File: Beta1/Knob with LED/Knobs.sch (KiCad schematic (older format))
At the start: 16 parts, among them U1000 MCP3008T-I/SL

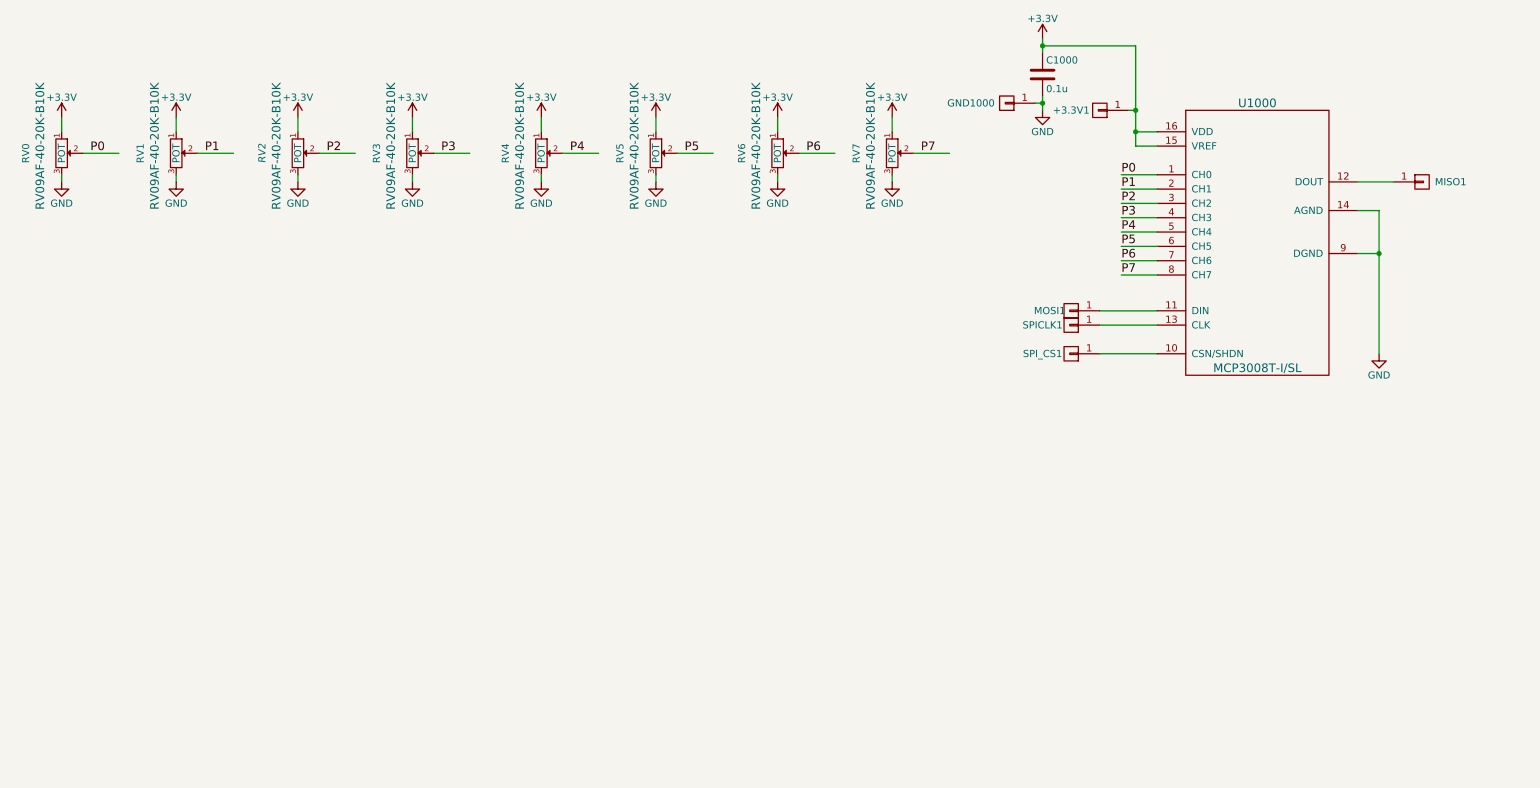
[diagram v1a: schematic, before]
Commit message: Duplicated row. Placed components and drill holes. Ready to be routed.
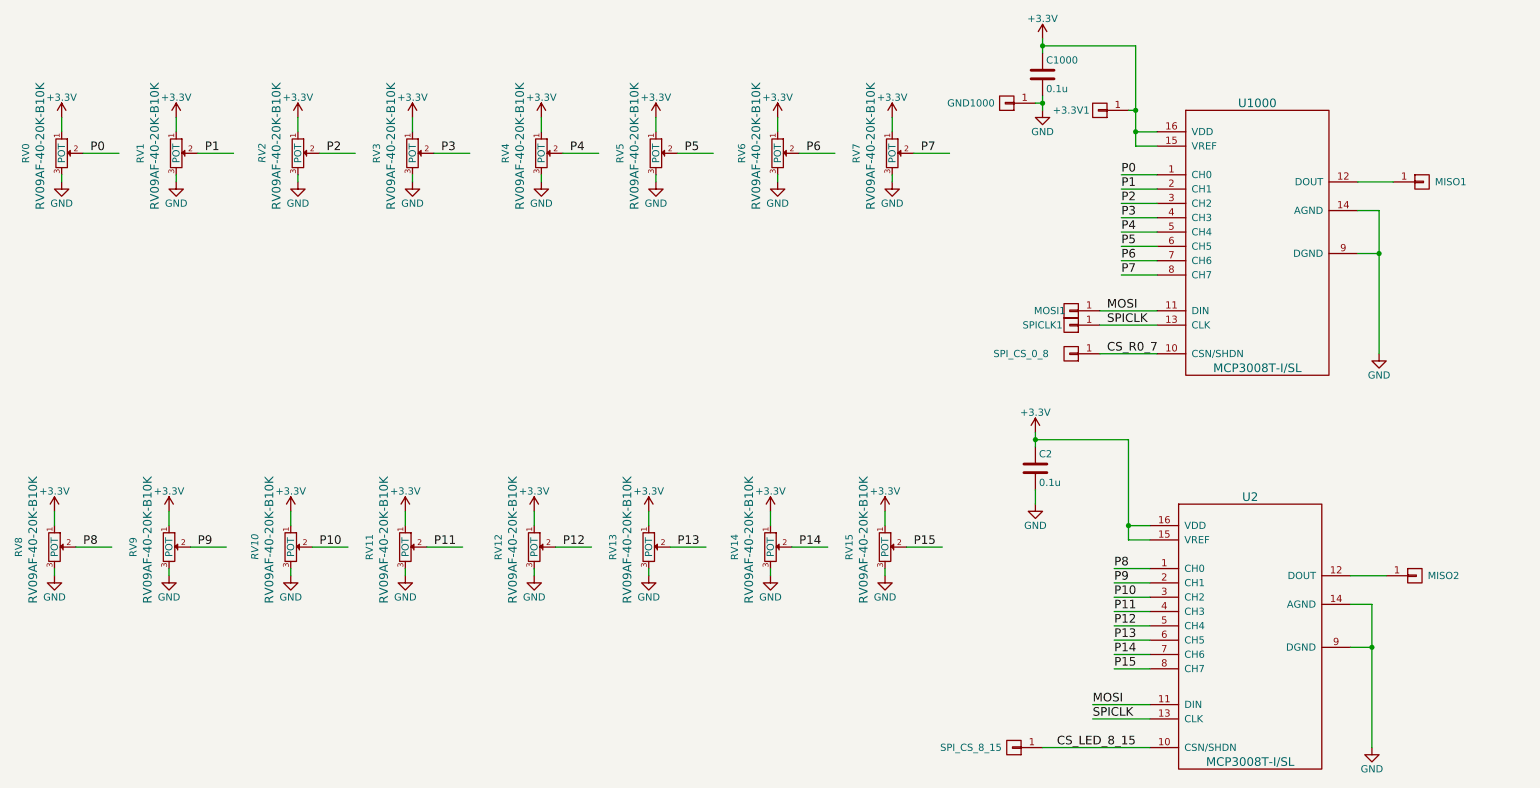
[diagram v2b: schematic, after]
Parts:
- added C2: 0.1u, Capacitors_SMD:C_0603, symbol C
- added MISO2, SPI_CS_8_15: CONN_01X01, Liberry:single_0.1, symbol CONN_01X01
- added RV10, RV11, RV12, RV13, RV14, RV15, RV8, RV9: POT, Liberry:RV09AF-40-20K-B10K, symbol POT
- added U2: MCP3008T-I/SL, Liberry:SOIC-16, symbol MCP3008T-I/SL
- renumbered SPI_CS1 to SPI_CS_0_8
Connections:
- net labels added: CS_LED_8_15, CS_R0_7, MOSI, P10, P11, P12, P13, P14, P15, P8, P9, SPICLK
- wire segments 47 -> 92

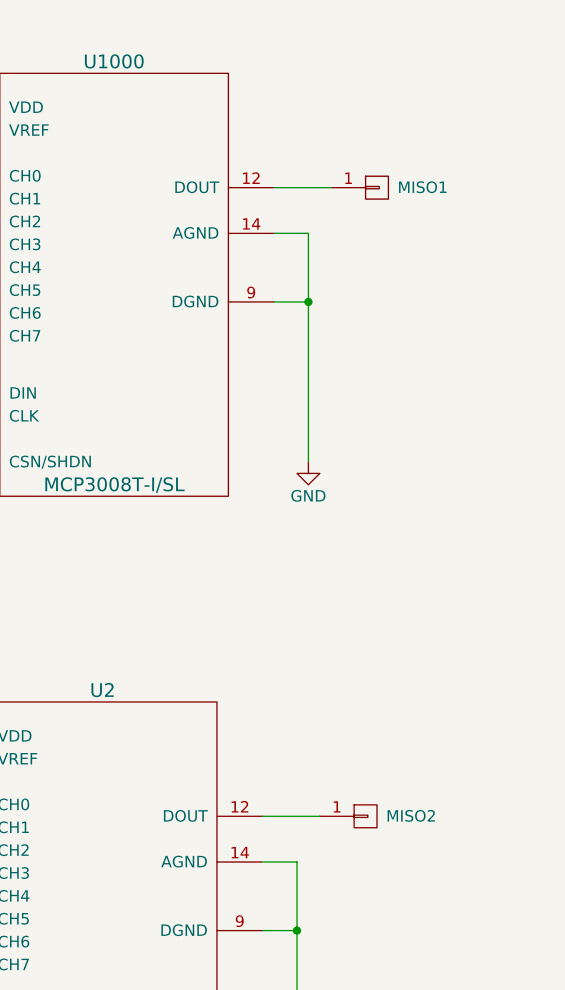
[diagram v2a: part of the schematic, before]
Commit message: Knob PCB is routed.
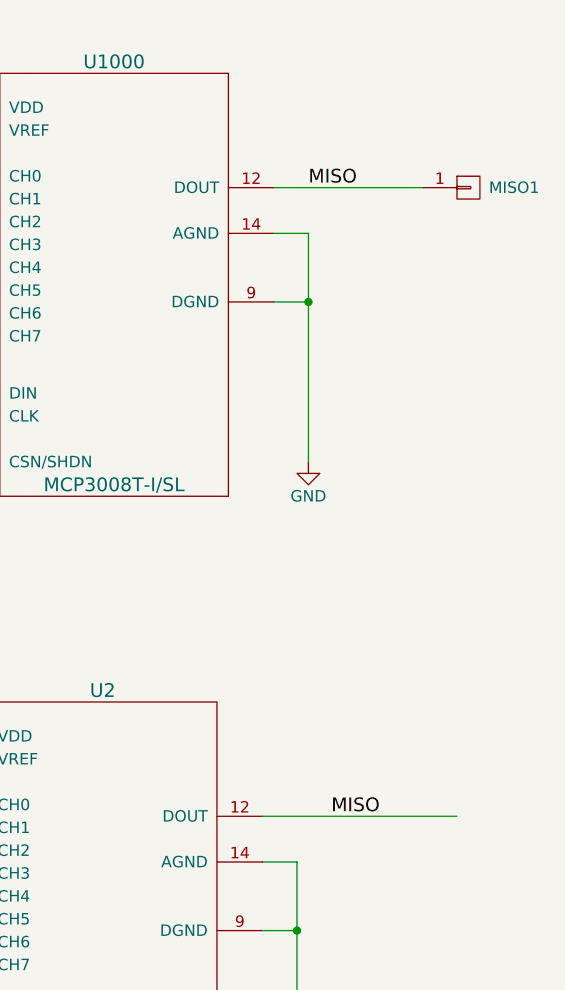
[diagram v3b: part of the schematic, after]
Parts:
- removed MISO2: CONN_01X01, Liberry:single_0.1, symbol CONN_01X01
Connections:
- net labels added: MISO
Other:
- moved on the sheet: MISO1
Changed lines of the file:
@@
 L CONN_01X01 MISO1
 U 1 1 582E561D
-P 11650 1750
-F 0 "MISO1" H 11850 1750 50  0000 C CNN
-F 1 "CONN_01X01" V 11750 1750 50  0001 C CNN
-F 2 "Liberry:single_0.1" H 11650 1750 50  0001 C CNN
-F 3 "" H 11650 1750 50  0000 C CNN
-F 4 "PCB" H 11650 1750 60  0001 C CNN "MFG"
-F 5 "ON_PCB" H 11650 1750 60  0001 C CNN "MPN"
-	1    11650 1750
+P 12050 1750
+F 0 "MISO1" H 12250 1750 50  0000 C CNN
+F 1 "CONN_01X01" V 12150 1750 50  0001 C CNN
+F 2 "Liberry:single_0.1" H 12050 1750 50  0001 C CNN
+F 3 "" H 12050 1750 50  0000 C CNN
+F 4 "PCB" H 12050 1750 60  0001 C CNN "MFG"
+F 5 "ON_PCB" H 12050 1750 60  0001 C CNN "MPN"
+	1    12050 1750
 	1    0    0    -1
 $EndComp
@@
 	-1   0    0    1
 $EndComp
-Wire Wire Line
-	2150 1400 2150 1300
-Wire Wire Line
-	2150 1750 2150 1700
-Wire Wire Line
-	2300 1550 2550 1550
-Wire Wire Line
-	2950 1400 2950 1300
-Wire Wire Line
-	2950 1750 2950 1700
-Wire Wire Line
-	3100 1550 3350 1550
-Wire Wire Line
-	3800 1400 3800 1300
-Wire Wire Line
-	3800 1750 3800 1700
-Wire Wire Line
-	3950 1550 4200 1550
-Wire Wire Line
-	4600 1400 4600 1300
-Wire Wire Line
-	4600 1750 4600 1700
-Wire Wire Line
-	4750 1550 5000 1550
-Wire Wire Line
-	5500 1400 5500 1300
-Wire Wire Line
-	5500 1750 5500 1700
-Wire Wire Line
-	5650 1550 5900 1550
-Wire Wire Line
-	6300 1400 6300 1300
-Wire Wire Line
-	6300 1750 6300 1700
-Wire Wire Line
-	6450 1550 6700 1550
-Wire Wire Line
-	7150 1400 7150 1300
-Wire Wire Line
-	7150 1750 7150 1700
-Wire Wire Line
-	7300 1550 7550 1550
-Wire Wire Line
-	7950 1400 7950 1300
-Wire Wire Line
-	7950 1750 7950 1700
-Wire Wire Line
-	8100 1550 8350 1550
-Wire Wire Line
-	9000 1150 9000 1250
-Wire Wire Line
-	9000 750  9000 850
-Wire Wire Line
-	9650 1500 9800 1500
-Wire Wire Line
-	9650 800  9650 1500
-Wire Wire Line
-	9650 1400 9800 1400
-Wire Wire Line
-	9000 800  9650 800
-Connection ~ 9000 800
-Connection ~ 9650 1400
-Wire Wire Line
-	9800 1700 9550 1700
-Wire Wire Line
-	9550 1800 9800 1800
-Wire Wire Line
-	9800 1900 9550 1900
-Wire Wire Line
-	9800 2000 9550 2000
-Wire Wire Line
-	9800 2100 9550 2100
-Wire Wire Line
-	9800 2200 9550 2200
-Wire Wire Line
-	9800 2300 9550 2300
-Wire Wire Line
-	9800 2400 9550 2400
-Wire Wire Line
-	11350 1950 11350 2950
-Wire Wire Line
-	11350 2250 11200 2250
-Wire Wire Line
-	11350 1950 11200 1950
-Connection ~ 11350 2250
-Wire Wire Line
-	9400 2950 9800 2950
-Wire Wire Line
-	9400 2750 9800 2750
-Wire Wire Line
-	9400 2650 9800 2650
-Wire Wire Line
-	11450 1750 11200 1750
-Wire Wire Line
-	9600 1250 9650 1250
-Connection ~ 9650 1250
-Wire Wire Line
-	8950 1200 9000 1200
-Connection ~ 9000 1200
 $Comp
 L POT RV8
@@
 	1    8800 5700
 	-1   0    0    1
-$EndComp
-$Comp
-L CONN_01X01 MISO2
-U 1 1 582F4198
-P 11600 4500
-F 0 "MISO2" H 11800 4500 50  0000 C CNN
-F 1 "CONN_01X01" V 11700 4500 50  0001 C CNN
-F 2 "Liberry:single_0.1" H 11600 4500 50  0001 C CNN
-F 3 "" H 11600 4500 50  0000 C CNN
-F 4 "PCB" H 11600 4500 60  0001 C CNN "MFG"
-F 5 "ON_PCB" H 11600 4500 60  0001 C CNN "MPN"
-	1    11600 4500
-	1    0    0    -1
 $EndComp
 Text Label 9500 4550 0    60   ~ 0
@@
 Text Label 9500 5150 0    60   ~ 0
 P15
-Wire Wire Line
-	2100 4150 2100 4050
-Wire Wire Line
-	2100 4500 2100 4450
-Wire Wire Line
-	2250 4300 2500 4300
-Wire Wire Line
-	2900 4150 2900 4050
-Wire Wire Line
-	2900 4500 2900 4450
-Wire Wire Line
-	3050 4300 3300 4300
-Wire Wire Line
-	3750 4150 3750 4050
-Wire Wire Line
-	3750 4500 3750 4450
-Wire Wire Line
-	3900 4300 4150 4300
-Wire Wire Line
-	4550 4150 4550 4050
-Wire Wire Line
-	4550 4500 4550 4450
-Wire Wire Line
-	4700 4300 4950 4300
-Wire Wire Line
-	5450 4150 5450 4050
-Wire Wire Line
-	5450 4500 5450 4450
-Wire Wire Line
-	5600 4300 5850 4300
-Wire Wire Line
-	6250 4150 6250 4050
-Wire Wire Line
-	6250 4500 6250 4450
-Wire Wire Line
-	6400 4300 6650 4300
-Wire Wire Line
-	7100 4150 7100 4050
-Wire Wire Line
-	7100 4500 7100 4450
-Wire Wire Line
-	7250 4300 7500 4300
-Wire Wire Line
-	7900 4150 7900 4050
-Wire Wire Line
-	7900 4500 7900 4450
-Wire Wire Line
-	8050 4300 8300 4300
-Wire Wire Line
-	8950 3900 8950 4000
-Wire Wire Line
-	8950 3500 8950 3600
-Wire Wire Line
-	9600 4250 9750 4250
-Wire Wire Line
-	9600 3550 9600 4250
-Wire Wire Line
-	9600 4150 9750 4150
-Wire Wire Line
-	8950 3550 9600 3550
-Connection ~ 8950 3550
-Connection ~ 9600 4150
-Wire Wire Line
-	9750 4450 9500 4450
-Wire Wire Line
-	9500 4550 9750 4550
-Wire Wire Line
-	9750 4650 9500 4650
-Wire Wire Line
-	9750 4750 9500 4750
-Wire Wire Line
-	9750 4850 9500 4850
-Wire Wire Line
-	9750 4950 9500 4950
-Wire Wire Line
-	9750 5050 9500 5050
-Wire Wire Line
-	9750 5150 9500 5150
-Wire Wire Line
-	11300 4700 11300 5700
-Wire Wire Line
-	11300 5000 11150 5000
-Wire Wire Line
-	11300 4700 11150 4700
-Connection ~ 11300 5000
-Wire Wire Line
-	9000 5700 9750 5700
-Wire Wire Line
-	9350 5500 9750 5500
-Wire Wire Line
-	9350 5400 9750 5400
-Wire Wire Line
-	11400 4500 11150 4500
 Text Label 9450 2650 0    60   ~ 0
 MOSI
@@
 Text Label 9100 5700 0    60   ~ 0
 CS_LED_8_15
+Text Label 11350 1750 0    60   ~ 0
+MISO
+Wire Wire Line
+	2150 1400 2150 1300
+Wire Wire Line
+	2150 1750 2150 1700
+Wire Wire Line
+	2300 1550 2550 1550
+Wire Wire Line
+	2950 1400 2950 1300
+Wire Wire Line
+	2950 1750 2950 1700
+Wire Wire Line
+	3100 1550 3350 1550
+Wire Wire Line
+	3800 1400 3800 1300
+Wire Wire Line
+	3800 1750 3800 1700
+Wire Wire Line
+	3950 1550 4200 1550
+Wire Wire Line
+	4600 1400 4600 1300
+Wire Wire Line
+	4600 1750 4600 1700
+Wire Wire Line
+	4750 1550 5000 1550
+Wire Wire Line
+	5500 1400 5500 1300
+Wire Wire Line
+	5500 1750 5500 1700
+Wire Wire Line
+	5650 1550 5900 1550
+Wire Wire Line
+	6300 1400 6300 1300
+Wire Wire Line
+	6300 1750 6300 1700
+Wire Wire Line
+	6450 1550 6700 1550
+Wire Wire Line
+	7150 1400 7150 1300
+Wire Wire Line
+	7150 1750 7150 1700
+Wire Wire Line
+	7300 1550 7550 1550
+Wire Wire Line
+	7950 1400 7950 1300
+Wire Wire Line
+	7950 1750 7950 1700
+Wire Wire Line
+	8100 1550 8350 1550
+Wire Wire Line
+	9000 1150 9000 1250
+Wire Wire Line
+	9000 750  9000 850
+Wire Wire Line
+	9650 1500 9800 1500
+Wire Wire Line
+	9650 800  9650 1500
+Wire Wire Line
+	9650 1400 9800 1400
+Wire Wire Line
+	9000 800  9650 800
+Connection ~ 9000 800
+Connection ~ 9650 1400
+Wire Wire Line
+	9800 1700 9550 1700
+Wire Wire Line
+	9550 1800 9800 1800
+Wire Wire Line
+	9800 1900 9550 1900
+Wire Wire Line
+	9800 2000 9550 2000
+Wire Wire Line
+	9800 2100 9550 2100
+Wire Wire Line
+	9800 2200 9550 2200
+Wire Wire Line
+	9800 2300 9550 2300
+Wire Wire Line
+	9800 2400 9550 2400
+Wire Wire Line
+	11350 1950 11350 2950
+Wire Wire Line
+	11350 2250 11200 2250
+Wire Wire Line
+	11350 1950 11200 1950
+Connection ~ 11350 2250
+Wire Wire Line
+	9400 2950 9800 2950
+Wire Wire Line
+	9400 2750 9800 2750
+Wire Wire Line
+	9400 2650 9800 2650
+Wire Wire Line
+	11200 1750 11850 1750
+Wire Wire Line
+	9600 1250 9650 1250
+Connection ~ 9650 1250
+Wire Wire Line
+	8950 1200 9000 1200
+Connection ~ 9000 1200
+Wire Wire Line
+	2100 4150 2100 4050
+Wire Wire Line
+	2100 4500 2100 4450
+Wire Wire Line
+	2250 4300 2500 4300
+Wire Wire Line
+	2900 4150 2900 4050
+Wire Wire Line
+	2900 4500 2900 4450
+Wire Wire Line
+	3050 4300 3300 4300
+Wire Wire Line
+	3750 4150 3750 4050
+Wire Wire Line
+	3750 4500 3750 4450
+Wire Wire Line
+	3900 4300 4150 4300
+Wire Wire Line
+	4550 4150 4550 4050
+Wire Wire Line
+	4550 4500 4550 4450
+Wire Wire Line
+	4700 4300 4950 4300
+Wire Wire Line
+	5450 4150 5450 4050
+Wire Wire Line
+	5450 4500 5450 4450
+Wire Wire Line
+	5600 4300 5850 4300
+Wire Wire Line
+	6250 4150 6250 4050
+Wire Wire Line
+	6250 4500 6250 4450
+Wire Wire Line
+	6400 4300 6650 4300
+Wire Wire Line
+	7100 4150 7100 4050
+Wire Wire Line
+	7100 4500 7100 4450
+Wire Wire Line
+	7250 4300 7500 4300
+Wire Wire Line
+	7900 4150 7900 4050
+Wire Wire Line
+	7900 4500 7900 4450
+Wire Wire Line
+	8050 4300 8300 4300
+Wire Wire Line
+	8950 3900 8950 4000
+Wire Wire Line
+	8950 3500 8950 3600
+Wire Wire Line
+	9600 4250 9750 4250
+Wire Wire Line
+	9600 3550 9600 4250
+Wire Wire Line
+	9600 4150 9750 4150
+Wire Wire Line
+	8950 3550 9600 3550
+Connection ~ 8950 3550
+Connection ~ 9600 4150
+Wire Wire Line
+	9750 4450 9500 4450
+Wire Wire Line
+	9500 4550 9750 4550
+Wire Wire Line
+	9750 4650 9500 4650
+Wire Wire Line
+	9750 4750 9500 4750
+Wire Wire Line
+	9750 4850 9500 4850
+Wire Wire Line
+	9750 4950 9500 4950
+Wire Wire Line
+	9750 5050 9500 5050
+Wire Wire Line
+	9750 5150 9500 5150
+Wire Wire Line
+	11300 4700 11300 5700
+Wire Wire Line
+	11300 5000 11150 5000
+Wire Wire Line
+	11300 4700 11150 4700
+Connection ~ 11300 5000
+Wire Wire Line
+	9000 5700 9750 5700
+Wire Wire Line
+	9350 5500 9750 5500
+Wire Wire Line
+	9350 5400 9750 5400
+Wire Wire Line
+	11150 4500 12000 4500
+Text Label 11450 4500 0    60   ~ 0
+MISO
 $EndSCHEMATC
